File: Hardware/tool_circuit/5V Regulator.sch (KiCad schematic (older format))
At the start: 9 parts, among them U2 TPS563211DRLR

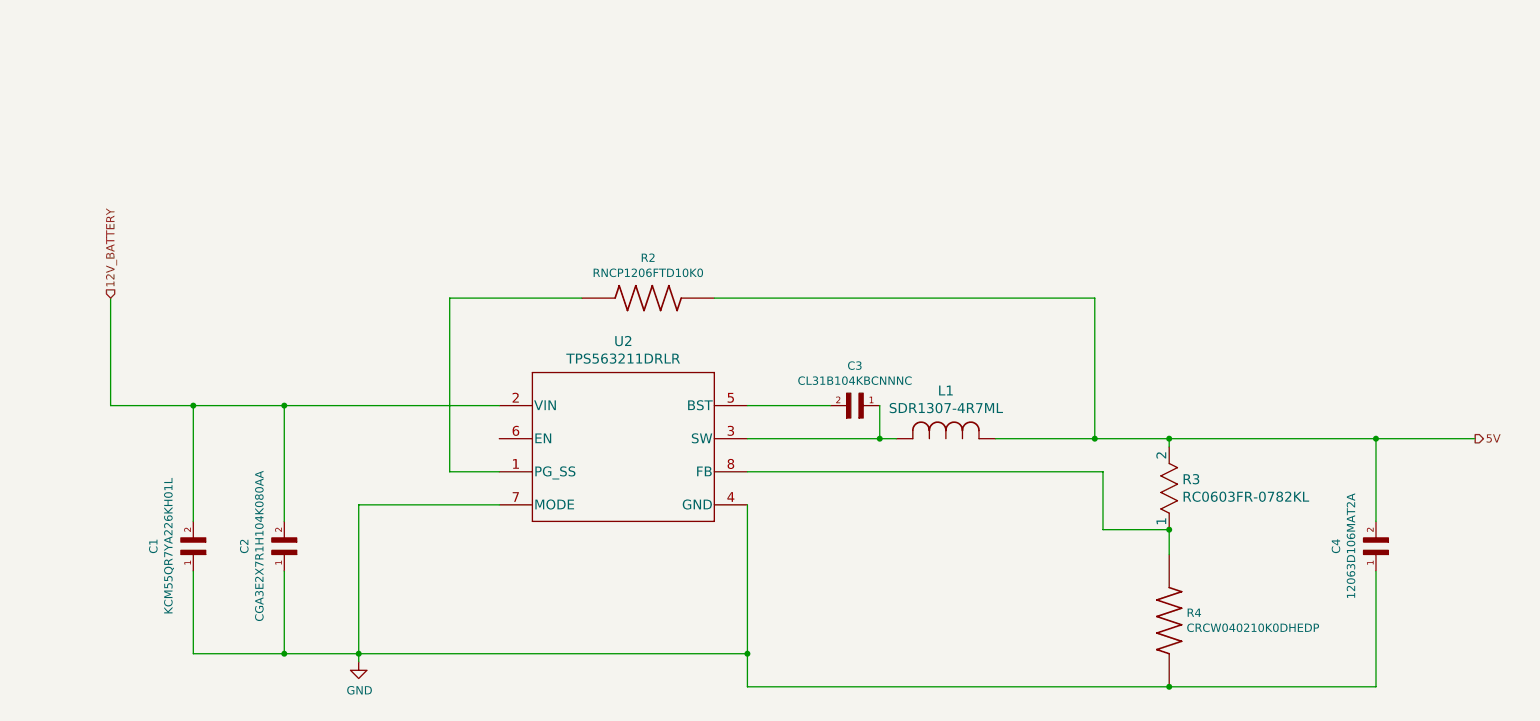
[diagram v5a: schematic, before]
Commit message: Tool Circuit schematic updates
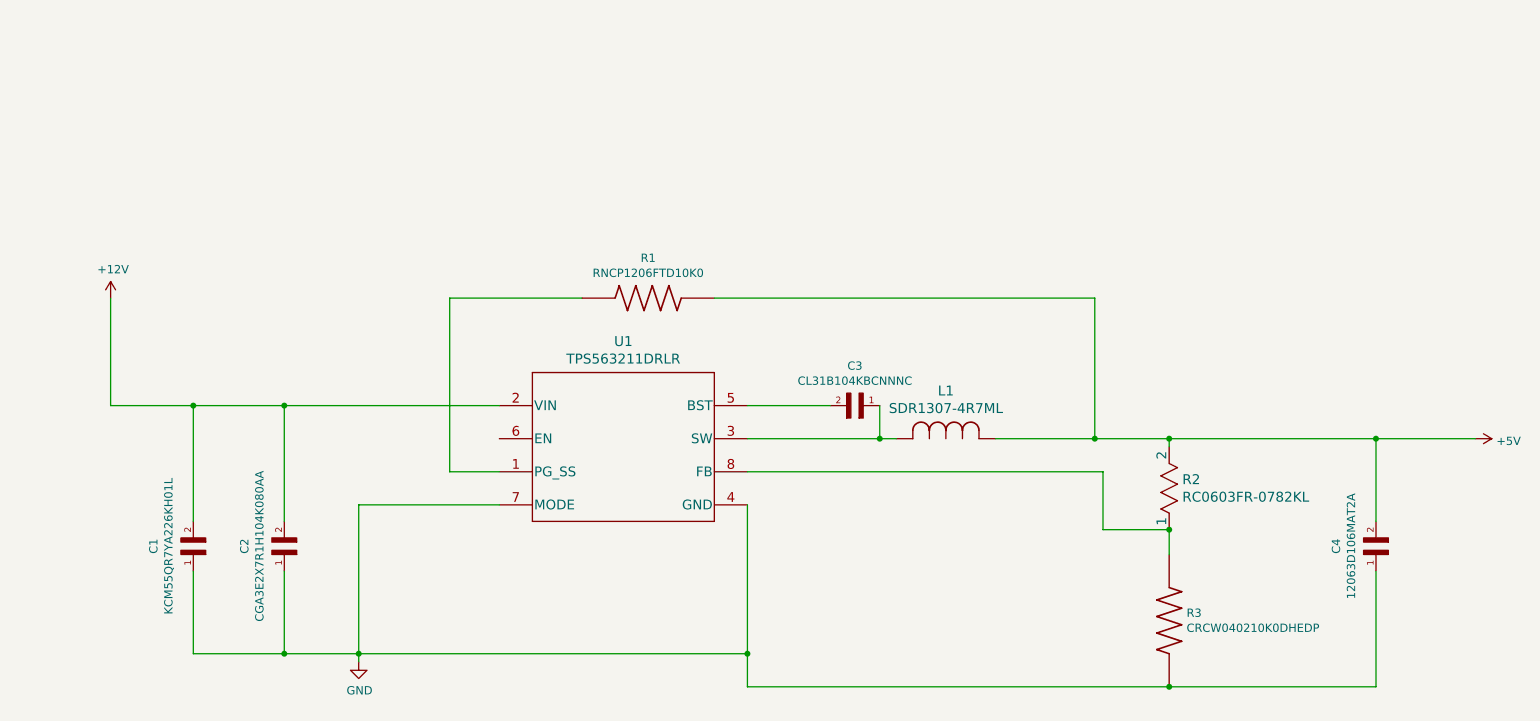
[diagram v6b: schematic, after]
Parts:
- renumbered R2 to R1, R3 to R2, R4 to R3, U2 to U1
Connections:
- net 12V_BATTERY renamed +12V
- net 5V renamed +5V
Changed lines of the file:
@@
 $Descr A4 11693 8268
 encoding utf-8
-Sheet 4 7
+Sheet 3 8
 Title ""
 Date ""
@@
 Comment4 ""
 $EndDescr
-Text HLabel 1950 2850 1    50   Input ~ 0
-12V_BATTERY
 Wire Wire Line
 	1950 2850 1950 3500
@@
 $EndComp
 $Comp
-L TPS563211DRLR:TPS563211DRLR U2
+L TPS563211DRLR:TPS563211DRLR U1
 U 1 1 61393280
 P 4300 3500
-F 0 "U2" H 5050 3888 60  0000 C CNN
+F 0 "U1" H 5050 3888 60  0000 C CNN
 F 1 "TPS563211DRLR" H 5050 3782 60  0000 C CNN
 F 2 "ul_TPS563211DRLR:TPS563211DRLR" H 4300 3440 60  0001 C CNN
@@
 	3000 3500 4300 3500
 $Comp
-L power:GND #PWR0107
+L power:GND #PWR02
 U 1 1 61401F04
 P 3450 5050
-F 0 "#PWR0107" H 3450 4800 50  0001 C CNN
+F 0 "#PWR02" H 3450 4800 50  0001 C CNN
 F 1 "GND" H 3455 4877 50  0000 C CNN
 F 2 "" H 3450 5050 50  0001 C CNN
@@
 	4000 2850 4800 2850
 $Comp
-L RNCP1206FTD10K0:RNCP1206FTD10K0 R2
+L RNCP1206FTD10K0:RNCP1206FTD10K0 R1
 U 1 1 61403723
 P 5200 2850
-F 0 "R2" H 5200 3092 50  0000 C CNN
+F 0 "R1" H 5200 3092 50  0000 C CNN
 F 1 "RNCP1206FTD10K0" H 5200 3001 50  0000 C CNN
 F 2 "RNCP1206FTD10K0:RESC3115X60N" H 5200 2850 50  0001 L BNN
@@
 	5800 5000 3450 5000
 $Comp
-L 2021-09-13_22-27-50:RC0603FR-0782KL R3
+L 2021-09-13_22-27-50:RC0603FR-0782KL R2
 U 1 1 6140CEA8
 P 8350 3750
-F 0 "R3" V 8547 3829 60  0000 L CNN
+F 0 "R2" V 8547 3829 60  0000 L CNN
 F 1 "RC0603FR-0782KL" V 8653 3829 60  0000 L CNN
 F 2 "ul_RC0603FR-0782KL:RC0603FR-0782KL" H 8600 3415 60  0001 C CNN
@@
 	7950 4250 8350 4250
 $Comp
-L CRCW040210K0DHEDP:CRCW040210K0DHEDP R4
+L CRCW040210K0DHEDP:CRCW040210K0DHEDP R3
 U 1 1 6140F8A3
 P 8350 4800
-F 0 "R4" V 8304 4905 50  0000 L CNN
+F 0 "R3" V 8304 4905 50  0000 L CNN
 F 1 "CRCW040210K0DHEDP" V 8395 4905 50  0000 L CNN
 F 2 "CRCW040210K0DHEDP:RESC1005X40N" H 8350 4800 50  0001 L BNN
@@
 	9600 5200 8350 5200
 Connection ~ 8350 5200
-Text HLabel 10200 3700 2    50   Output ~ 0
-5V
 Wire Wire Line
 	9600 3700 10200 3700
 Connection ~ 9600 3700
+$Comp
+L power:+12V #PWR01
+U 1 1 614E38F8
+P 1950 2850
+F 0 "#PWR01" H 1950 2700 50  0001 C CNN
+F 1 "+12V" H 1965 3023 50  0000 C CNN
+F 2 "" H 1950 2850 50  0001 C CNN
+F 3 "" H 1950 2850 50  0001 C CNN
+	1    1950 2850
+	1    0    0    -1
+$EndComp
+$Comp
+L power:+5V #PWR03
+U 1 1 614E7ADA
+P 10200 3700
+F 0 "#PWR03" H 10200 3550 50  0001 C CNN
+F 1 "+5V" V 10215 3828 50  0000 L CNN
+F 2 "" H 10200 3700 50  0001 C CNN
+F 3 "" H 10200 3700 50  0001 C CNN
+	1    10200 3700
+	0    1    1    0
+$EndComp
 $EndSCHEMATC

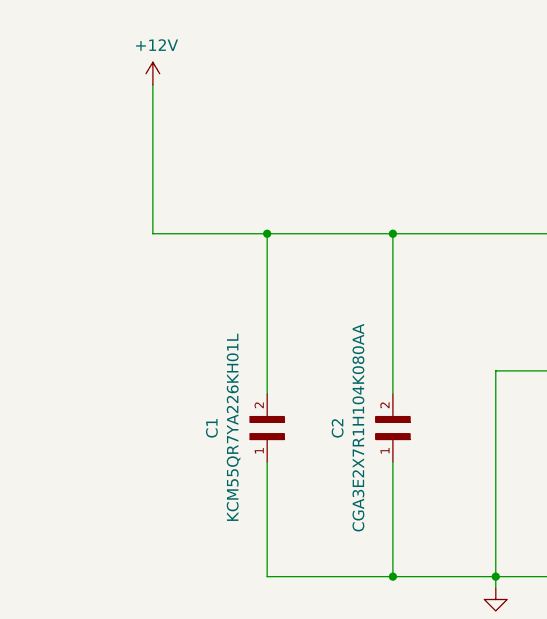
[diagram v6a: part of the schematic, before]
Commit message: schematic LEDs + switch
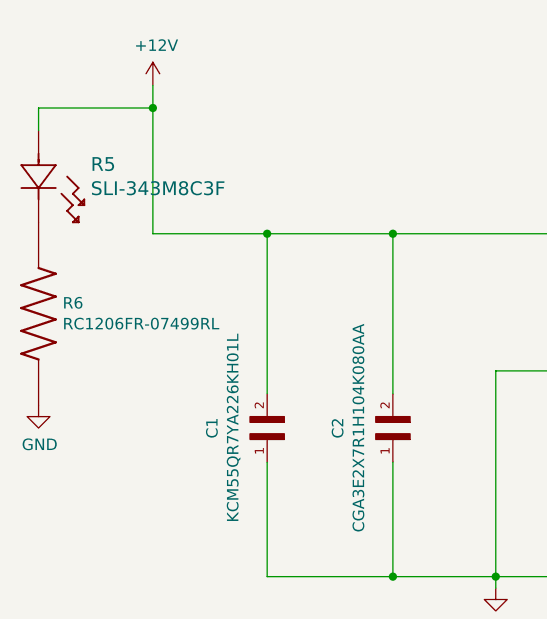
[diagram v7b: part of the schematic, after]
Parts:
- added R5: SLI-343M8C3F, LED_SLI-343D_ROM, symbol 2021-09-28_17-40-03:SLI-343M8C3F
- added R6: RC1206FR-07499RL, RESC3116X65N, symbol RC1206FR-07499RL:RC1206FR-07499RL
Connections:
- net +12V: now also R5.2
- net GND: now also R6.2
- new net: R5.1, R6.1
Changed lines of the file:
@@
 $EndDescr
 Wire Wire Line
-	1950 2850 1950 3500
+	1950 2850 1950 2950
 $Comp
 L KCM55QR7YA226KH01L:KCM55QR7YA226KH01L C1
@@
 	9600 5200 8350 5200
 Connection ~ 8350 5200
-Wire Wire Line
-	9600 3700 10200 3700
 Connection ~ 9600 3700
 $Comp
@@
 	0    1    1    0
 $EndComp
+$Comp
+L 2021-09-28_17-40-03:SLI-343M8C3F R5
+U 1 1 6156F04F
+P 1450 3050
+F 0 "R5" V 1597 3278 60  0000 L CNN
+F 1 "SLI-343M8C3F" V 1703 3278 60  0000 L CNN
+F 2 "LED_SLI-343D_ROM" H 1650 2690 60  0001 C CNN
+F 3 "" H 1450 3050 60  0000 C CNN
+	1    1450 3050
+	0    1    1    0
+$EndComp
+Wire Wire Line
+	1950 2950 1450 2950
+Wire Wire Line
+	1450 2950 1450 3050
+Connection ~ 1950 2950
+Wire Wire Line
+	1950 2950 1950 3500
+Wire Wire Line
+	9600 3700 10200 3700
+$Comp
+L RC1206FR-07499RL:RC1206FR-07499RL R6
+U 1 1 615AAF1C
+P 1450 3850
+F 0 "R6" V 1404 3955 50  0000 L CNN
+F 1 "RC1206FR-07499RL" V 1495 3955 50  0000 L CNN
+F 2 "RESC3116X65N" H 1450 3850 50  0001 L BNN
+F 3 "" H 1450 3850 50  0001 L BNN
+	1    1450 3850
+	0    1    1    0
+$EndComp
+$Comp
+L power:GND #PWR0101
+U 1 1 615ABBAB
+P 1450 4250
+F 0 "#PWR0101" H 1450 4000 50  0001 C CNN
+F 1 "GND" H 1455 4077 50  0000 C CNN
+F 2 "" H 1450 4250 50  0001 C CNN
+F 3 "" H 1450 4250 50  0001 C CNN
+	1    1450 4250
+	1    0    0    -1
+$EndComp
 $EndSCHEMATC

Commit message: Latest revisions to schematic
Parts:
- removed C2: CGA3E2X7R1H104K080AA, CGA3E2X7R1H104K080AA:CAPC1608X90N, symbol CGA3E2X7R1H104K080AA:CGA3E2X7R1H104K080AA
- removed R6: RC1206FR-07499RL, RESC3116X65N, symbol RC1206FR-07499RL:RC1206FR-07499RL
- added C?: 0.1UF, CAPC3216X180N, symbol CL31B104KBCNNNC:CL31B104KBCNNNC
- added R?: 820, RESC3115X65N, symbol CRGCQ1206F820R:CRGCQ1206F820R
- added R?: 0, RES_RK73Z2B_KOA, symbol 2021-10-08_20-10-06:RK73Z2BTTD
- added TP? (x2): S2751-46R, HARWIN_S2751-46R, symbol S2751-46R:S2751-46R
- C1: value KCM55QR7YA226KH01L -> 22UF
- C3: value CL31B104KBCNNNC -> 0.1UF
- C4: value 12063D106MAT2A -> 10UF
- L1: value SDR1307-4R7ML -> 4.7UH
- R1: value RNCP1206FTD10K0 -> 10K
- R2: value RC0603FR-0782KL -> 82K
- R3: value CRCW040210K0DHEDP -> 10K
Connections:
- net +12V: now also C?.2, TP?.1
- net +5V: now also TP?.1
- net GND: now also C?.1, R?.2, R?.2
- net at U1.6 (EN): now also R?.1
- net at R5.1: now also R?.1
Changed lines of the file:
@@
 encoding utf-8
 Sheet 3 8
-Title ""
+Title "12V-5V Regulator"
 Date ""
 Rev ""
@@
 P 2450 4400
 F 0 "C1" H 2500 4640 50  0000 C CNN
-F 1 "KCM55QR7YA226KH01L" H 2500 4549 50  0000 C CNN
+F 1 "22UF" H 2500 4549 50  0000 C CNN
 F 2 "KCM55QR7YA226KH01L:CAPC6153X390N" H 2450 4400 50  0001 L BNN
 F 3 "https://www.snapeda.com/parts/KCM55QR7YA226KH01L/Murata%20Electronics/view-part/1365129/?welcome=home&ref=search&t=KCM55QR7YA226KH01L#" H 2450 4400 50  0001 L BNN
@@
 $EndComp
 $Comp
-L CGA3E2X7R1H104K080AA:CGA3E2X7R1H104K080AA C2
-U 1 1 61326D86
-P 3000 4400
-F 0 "C2" H 3050 4640 50  0000 C CNN
-F 1 "CGA3E2X7R1H104K080AA" H 3050 4549 50  0000 C CNN
-F 2 "CGA3E2X7R1H104K080AA:CAPC1608X90N" H 3000 4400 50  0001 L BNN
-F 3 "" H 3000 4400 50  0001 L BNN
-	1    3000 4400
-	0    -1   -1   0
-$EndComp
-$Comp
 L 12063D106MAT2A:12063D106MAT2A C4
 U 1 1 613292F8
 P 9600 4400
 F 0 "C4" H 9650 4640 50  0000 C CNN
-F 1 "12063D106MAT2A" H 9650 4549 50  0000 C CNN
+F 1 "10UF" H 9650 4549 50  0000 C CNN
 F 2 "12063D106MAT2A:CAPC3216X178N" H 9600 4400 50  0001 L BNN
 F 3 "" H 9600 4400 50  0001 L BNN
@@
 P 6400 3500
 F 0 "C3" H 6450 3740 50  0000 C CNN
-F 1 "CL31B104KBCNNNC" H 6450 3649 50  0000 C CNN
+F 1 "0.1UF" H 6450 3649 50  0000 C CNN
 F 2 "CL31B104KBCNNNC:CAPC3216X180N" H 6400 3500 50  0001 L BNN
 F 3 "" H 6400 3500 50  0001 L BNN
@@
 Connection ~ 2450 3500
 Wire Wire Line
-	2450 3500 3000 3500
-Wire Wire Line
 	3000 4200 3000 3500
 Connection ~ 3000 3500
 Wire Wire Line
 	3000 3500 4300 3500
-$Comp
-L power:GND #PWR02
-U 1 1 61401F04
-P 3450 5050
-F 0 "#PWR02" H 3450 4800 50  0001 C CNN
-F 1 "GND" H 3455 4877 50  0000 C CNN
-F 2 "" H 3450 5050 50  0001 C CNN
-F 3 "" H 3450 5050 50  0001 C CNN
-	1    3450 5050
-	1    0    0    -1
-$EndComp
 Wire Wire Line
 	3000 4500 3000 5000
 Wire Wire Line
-	3000 5000 3450 5000
-Wire Wire Line
-	3450 5000 3450 5050
+	3000 5000 3300 5000
+Wire Wire Line
+	4100 5000 4100 5050
 Wire Wire Line
 	2450 4500 2450 5000
@@
 Connection ~ 3000 5000
 Wire Wire Line
-	4300 4100 3450 4100
-Wire Wire Line
-	3450 4100 3450 5000
-Connection ~ 3450 5000
+	4300 4100 4100 4100
+Wire Wire Line
+	4100 4100 4100 5000
 Wire Wire Line
 	4300 3900 4000 3900
@@
 P 5200 2850
 F 0 "R1" H 5200 3092 50  0000 C CNN
-F 1 "RNCP1206FTD10K0" H 5200 3001 50  0000 C CNN
+F 1 "10K" H 5200 3001 50  0000 C CNN
 F 2 "RNCP1206FTD10K0:RESC3115X60N" H 5200 2850 50  0001 L BNN
 F 3 "" H 5200 2850 50  0001 L BNN
@@
 P 6700 3700
 F 0 "L1" H 7000 3989 60  0000 C CNN
-F 1 "SDR1307-4R7ML" H 7000 3883 60  0000 C CNN
+F 1 "4.7UH" H 7000 3883 60  0000 C CNN
 F 2 "ul_SDR1307-4R7ML:SDR1307-4R7ML" H 6975 3415 60  0001 C CNN
 F 3 "" H 6700 3700 60  0000 C CNN
@@
 Wire Wire Line
 	5800 4100 5800 5000
-Wire Wire Line
-	5800 5000 3450 5000
 $Comp
 L 2021-09-13_22-27-50:RC0603FR-0782KL R2
@@
 P 8350 3750
 F 0 "R2" V 8547 3829 60  0000 L CNN
-F 1 "RC0603FR-0782KL" V 8653 3829 60  0000 L CNN
+F 1 "82K" V 8653 3829 60  0000 L CNN
 F 2 "ul_RC0603FR-0782KL:RC0603FR-0782KL" H 8600 3415 60  0001 C CNN
 F 3 "" H 8350 3750 60  0000 C CNN
@@
 P 8350 4800
 F 0 "R3" V 8304 4905 50  0000 L CNN
-F 1 "CRCW040210K0DHEDP" V 8395 4905 50  0000 L CNN
+F 1 "10K" V 8395 4905 50  0000 L CNN
 F 2 "CRCW040210K0DHEDP:RESC1005X40N" H 8350 4800 50  0001 L BNN
 F 3 "" H 8350 4800 50  0001 L BNN
@@
 	9600 3700 10200 3700
 $Comp
-L RC1206FR-07499RL:RC1206FR-07499RL R6
-U 1 1 615AAF1C
-P 1450 3850
-F 0 "R6" V 1404 3955 50  0000 L CNN
-F 1 "RC1206FR-07499RL" V 1495 3955 50  0000 L CNN
-F 2 "RESC3116X65N" H 1450 3850 50  0001 L BNN
-F 3 "" H 1450 3850 50  0001 L BNN
-	1    1450 3850
-	0    1    1    0
-$EndComp
-$Comp
 L power:GND #PWR0101
 U 1 1 615ABBAB
@@
 	1    0    0    -1
 $EndComp
+$Comp
+L CRGCQ1206F820R:CRGCQ1206F820R R?
+U 1 1 615F0A81
+P 1450 3850
+F 0 "R?" V 1404 3955 50  0000 L CNN
+F 1 "820" V 1495 3955 50  0000 L CNN
+F 2 "RESC3115X65N" H 1450 3850 50  0001 L BNN
+F 3 "" H 1450 3850 50  0001 L BNN
+F 4 "2-2176343-4" H 1450 3850 50  0001 L BNN "Comment"
+	1    1450 3850
+	0    1    1    0
+$EndComp
+$Comp
+L 2021-10-08_20-10-06:RK73Z2BTTD R?
+U 1 1 616405FD
+P 3300 4000
+F 0 "R?" V 3497 4079 60  0000 L CNN
+F 1 "0" V 3603 4079 60  0000 L CNN
+F 2 "RES_RK73Z2B_KOA" H 3550 3665 60  0001 C CNN
+F 3 "" H 3300 4000 60  0000 C CNN
+	1    3300 4000
+	0    1    1    0
+$EndComp
+Wire Wire Line
+	4300 3700 3300 3700
+Wire Wire Line
+	3300 3700 3300 4000
+Wire Wire Line
+	3300 4500 3300 5000
+Connection ~ 3300 5000
+Connection ~ 4100 5000
+$Comp
+L power:GND #PWR02
+U 1 1 61401F04
+P 4100 5050
+F 0 "#PWR02" H 4100 4800 50  0001 C CNN
+F 1 "GND" H 4105 4877 50  0000 C CNN
+F 2 "" H 4100 5050 50  0001 C CNN
+F 3 "" H 4100 5050 50  0001 C CNN
+	1    4100 5050
+	1    0    0    -1
+$EndComp
+Wire Wire Line
+	3300 5000 4100 5000
+Wire Wire Line
+	4100 5000 5800 5000
+$Comp
+L CL31B104KBCNNNC:CL31B104KBCNNNC C?
+U 1 1 6164A2E7
+P 3000 4300
+F 0 "C?" V 3004 4403 50  0000 L CNN
+F 1 "0.1UF" V 3095 4403 50  0000 L CNN
+F 2 "CAPC3216X180N" H 3000 4300 50  0001 L BNN
+F 3 "" H 3000 4300 50  0001 L BNN
+	1    3000 4300
+	0    1    1    0
+$EndComp
+Text Label 1500 2950 0    50   ~ 0
+12V_LED
+$Comp
+L S2751-46R:S2751-46R TP?
+U 1 1 6164D605
+P 3000 3400
+F 0 "TP?" H 3085 3467 50  0000 L CNN
+F 1 "S2751-46R" H 3085 3376 50  0000 L CNN
+F 2 "HARWIN_S2751-46R" H 3000 3400 50  0001 L BNN
+F 3 "" H 3000 3400 50  0001 L BNN
+F 4 "HARWIN" H 3000 3400 50  0001 L BNN "MANUFACTURER"
+F 5 "Manufacturer Recommendations" H 3000 3400 50  0001 L BNN "STANDARD"
+F 6 "" H 3000 3400 50  0001 L BNN "PARTREV"
+	1    3000 3400
+	1    0    0    -1
+$EndComp
+Wire Wire Line
+	2450 3500 3000 3500
+$Comp
+L S2751-46R:S2751-46R TP?
+U 1 1 6164FDC2
+P 8350 3600
+F 0 "TP?" H 8435 3667 50  0000 L CNN
+F 1 "S2751-46R" H 8435 3576 50  0000 L CNN
+F 2 "HARWIN_S2751-46R" H 8350 3600 50  0001 L BNN
+F 3 "" H 8350 3600 50  0001 L BNN
+F 4 "HARWIN" H 8350 3600 50  0001 L BNN "MANUFACTURER"
+F 5 "Manufacturer Recommendations" H 8350 3600 50  0001 L BNN "STANDARD"
+F 6 "" H 8350 3600 50  0001 L BNN "PARTREV"
+	1    8350 3600
+	1    0    0    -1
+$EndComp
